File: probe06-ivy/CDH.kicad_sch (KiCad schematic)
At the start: 38 parts, among them J2 Conn_Coaxial, Q1 S9014, U4 NEO-M8M, U5 XBP9B-DPST-001, U6 24LC32, U7 BMP280

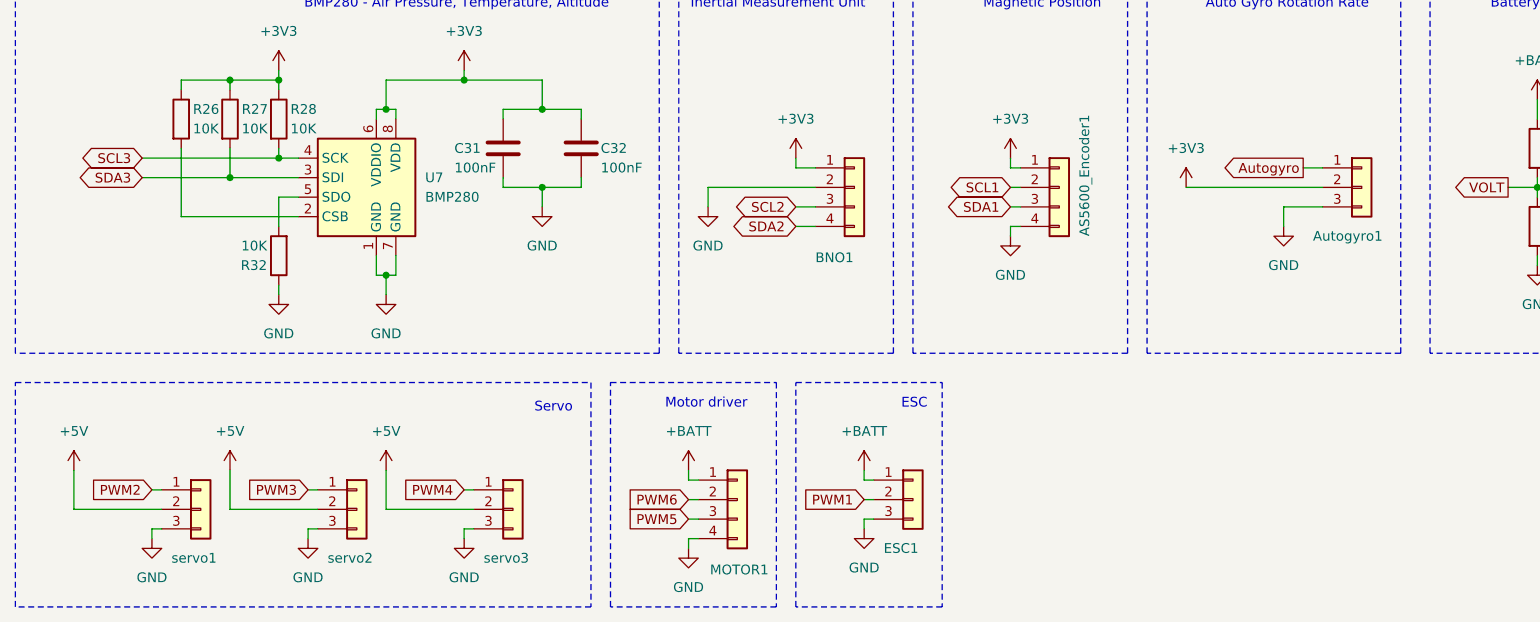
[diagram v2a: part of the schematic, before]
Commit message: Routing (3) Signal routing mostly done with something that needs TODO next: - Correction for power signals - Tidy up component silkscreen - Add team name and tagline
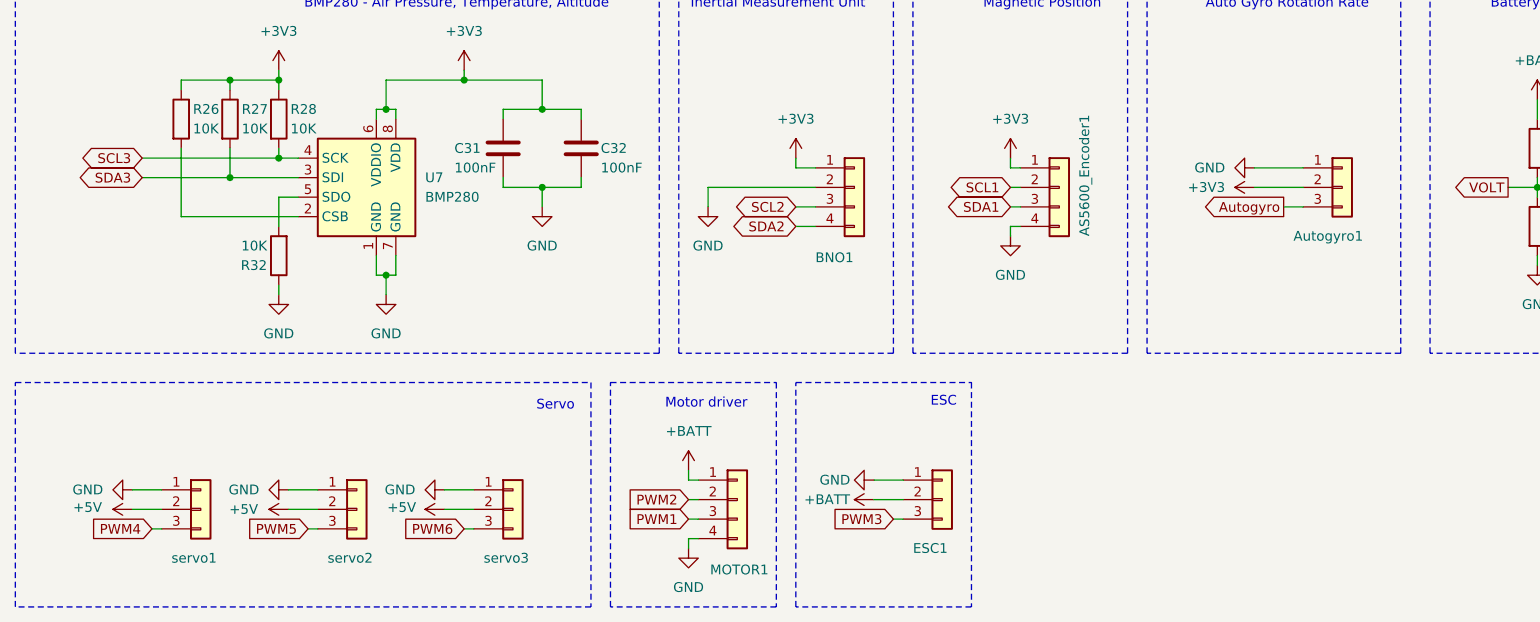
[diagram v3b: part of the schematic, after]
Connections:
- net +BATT: now also ESC1.2 (Pin_2); no longer ESC1.1 (Pin_1)
- net Autogyro: now also Autogyro1.3 (Pin_3); no longer Autogyro1.1 (Pin_1)
- net GND: now also Autogyro1.1 (Pin_1), ESC1.1 (Pin_1), servo1.1 (Pin_1), servo2.1 (Pin_1), servo3.1 (Pin_1); no longer Autogyro1.3 (Pin_3), ESC1.3 (Pin_3), servo1.3 (Pin_3), servo2.3 (Pin_3), servo3.3 (Pin_3)
- net PWM1: now also MOTOR1.3 (Pin_3); no longer ESC1.2 (Pin_2)
- net PWM2: now also MOTOR1.2 (Pin_2); no longer servo1.1 (Pin_1)
- net PWM3: now also ESC1.3 (Pin_3); no longer servo2.1 (Pin_1)
- net PWM4: now also servo1.3 (Pin_3); no longer servo3.1 (Pin_1)
- net PWM5: now also servo2.3 (Pin_3); no longer MOTOR1.3 (Pin_3)
- net PWM6: now also servo3.3 (Pin_3); no longer MOTOR1.2 (Pin_2)
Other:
- moved on the sheet: Autogyro1, ESC1

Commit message: rev 1.2
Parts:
- removed D11: D, Diode_SMD:D_SOD-123, symbol Device:D
- removed R18: 1K, Resistor_SMD:R_0603_1608Metric, symbol Device:R
- renumbered D12 to D10, R19 to R18, R20 to R19, R21 to R20, R22 to R21, R23 to R22, R24 to R23, R25 to R24, R26 to R25, R27 to R26, R28 to R27, R29 to R28, R30 to R29, R31 to R30, R32 to R31

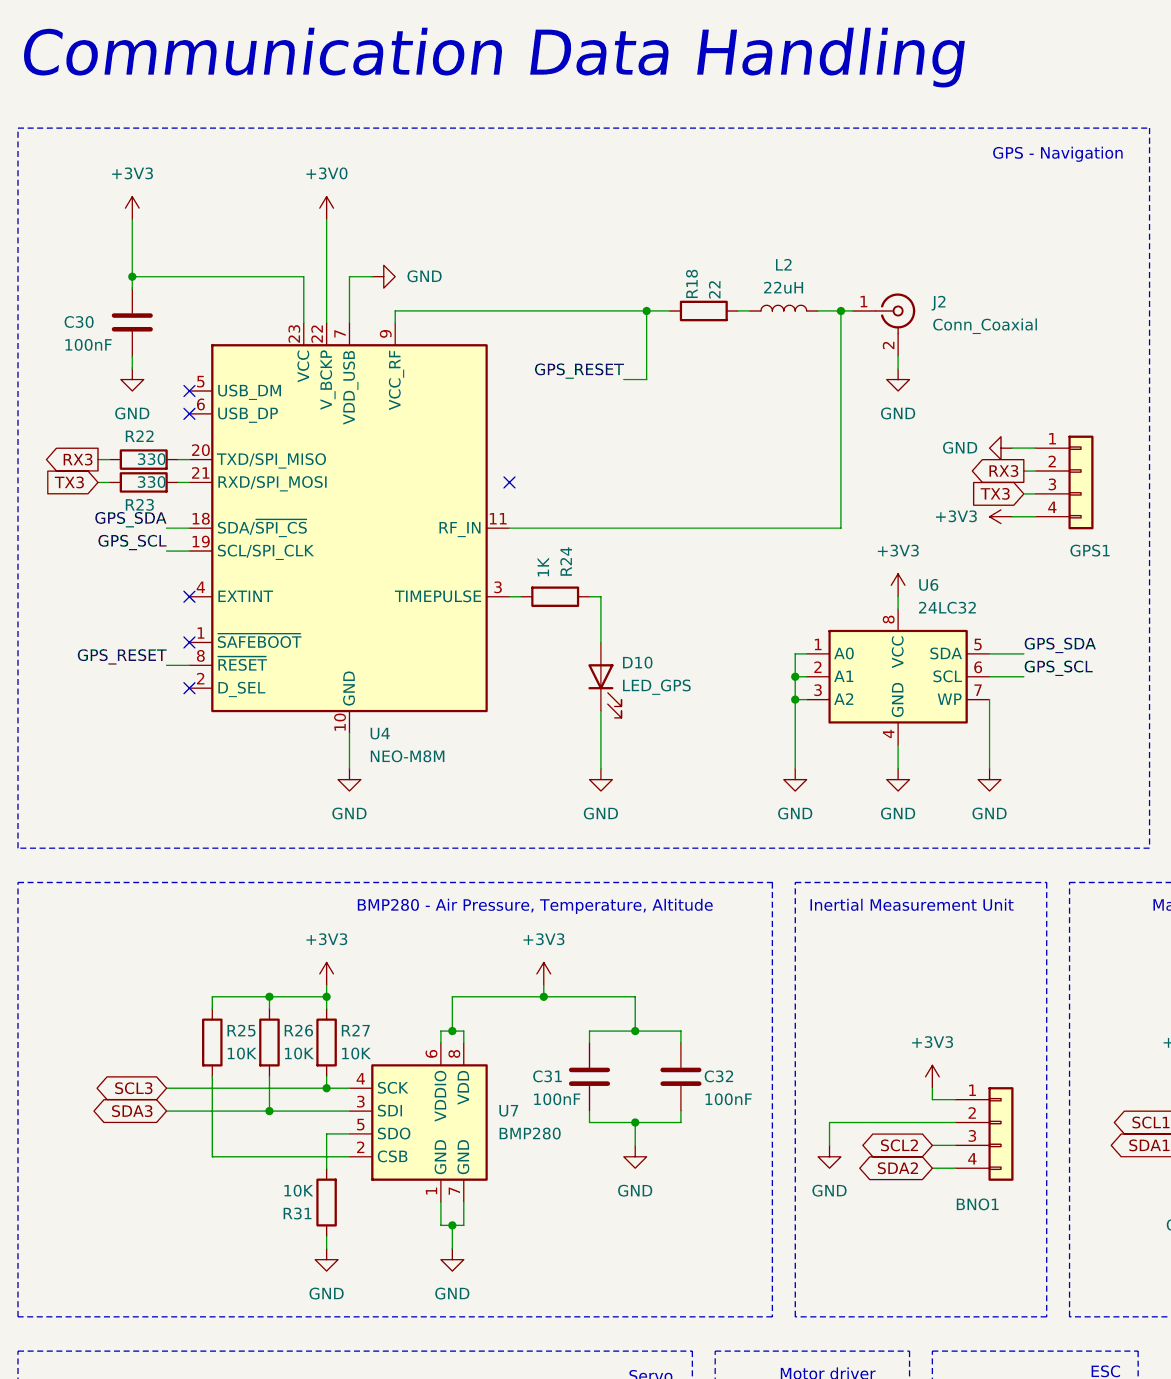
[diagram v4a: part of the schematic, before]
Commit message: rev 1.2.1 add additional pin
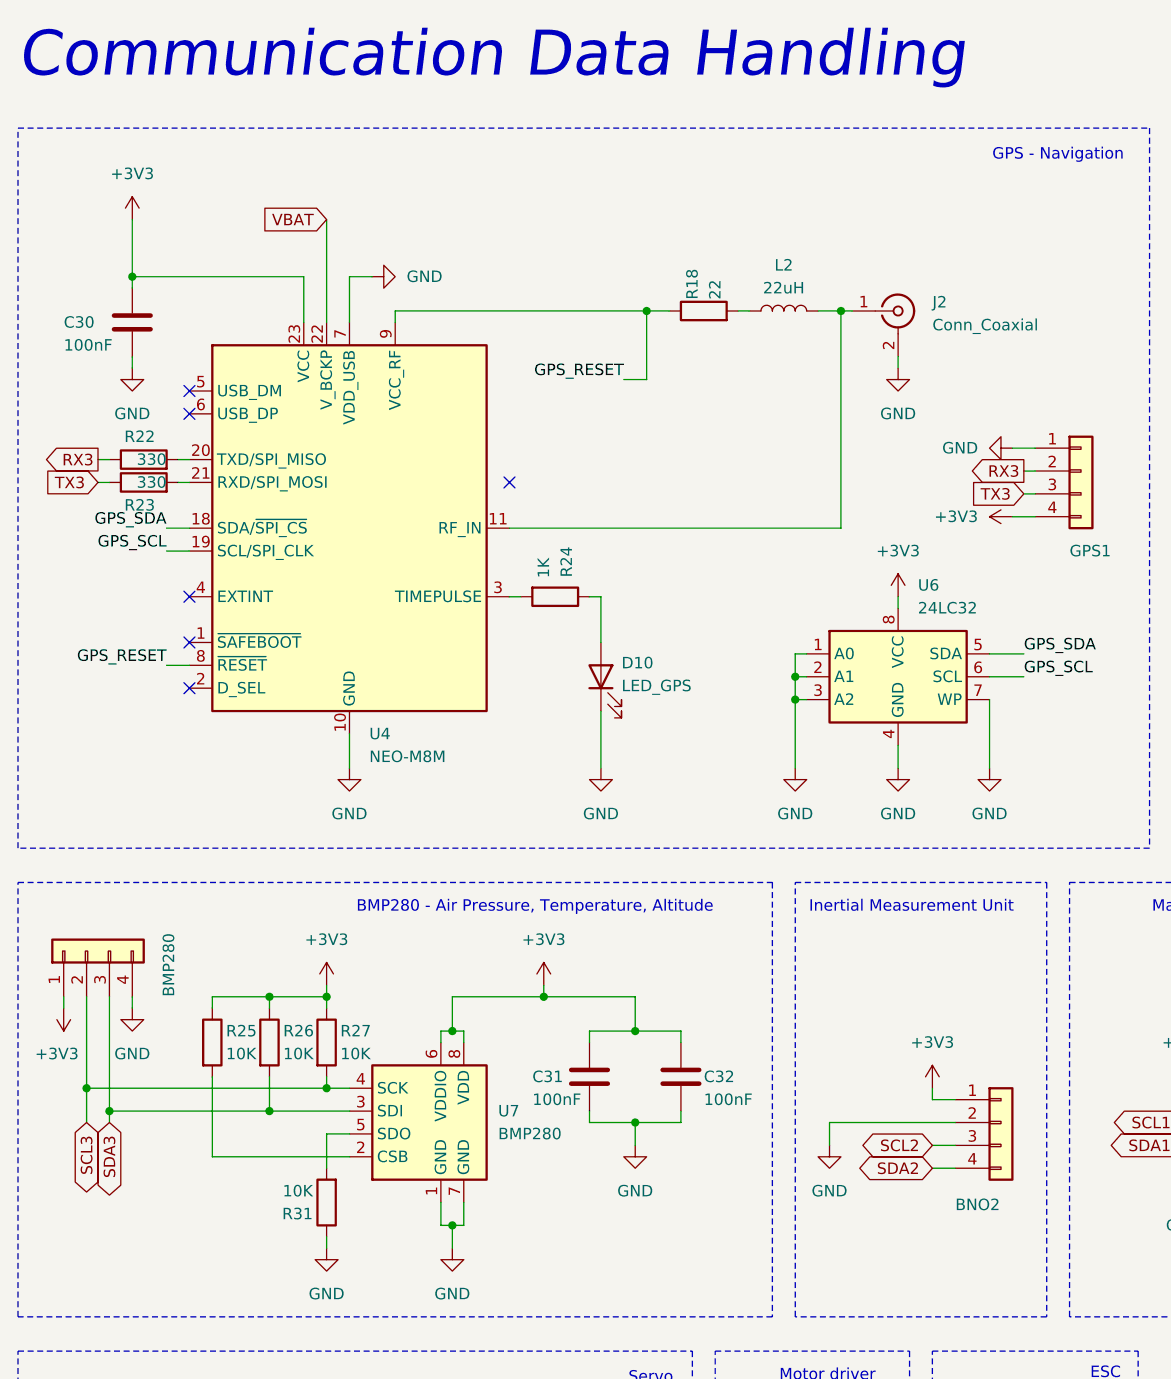
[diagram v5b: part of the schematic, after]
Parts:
- added BMP280: xx, Connector_PinHeader_2.54mm:PinHeader_1x04_P2.54mm_Vertical, symbol Connector_Generic:Conn_01x04
- renumbered BNO1 to BNO2
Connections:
- net +3V3: now also BMP280.1 (Pin_1)
- net GND: now also BMP280.4 (Pin_4)
- net SCL3: now also BMP280.2 (Pin_2)
- net SDA3: now also BMP280.3 (Pin_3)
- net +3V0 renamed VBAT

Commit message: mboh
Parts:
- removed R22, R23: 330, Resistor_SMD:R_0603_1608Metric, symbol Device:R
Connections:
- net RX3: now also U4.20 (TXD/SPI_MISO)
- net TX3: now also U4.21 (RXD/SPI_MOSI)
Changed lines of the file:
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@@
 	(wire
 		(pts
-			(xy 34.29 68.58) (xy 35.56 68.58)
-		)
-		(stroke
-			(width 0)
-			(type default)
-		)
-	)
-	(wire
-		(pts
 			(xy 90.17 130.81) (xy 90.17 129.54)
 		)
@@
 	(wire
 		(pts
-			(xy 25.4 68.58) (xy 26.67 68.58)
+			(xy 25.4 68.58) (xy 35.56 68.58)
 		)
 		(stroke
@@
 	(wire
 		(pts
-			(xy 25.4 66.04) (xy 26.67 66.04)
+			(xy 25.4 66.04) (xy 35.56 66.04)
 		)
 		(stroke
@@
 	(wire
 		(pts
-			(xy 34.29 66.04) (xy 35.56 66.04)
-		)
-		(stroke
-			(width 0)
-			(type default)
-		)
-	)
-	(wire
-		(pts
 			(xy 26.67 138.43) (xy 44.45 138.43)
 		)
@@
 	)
 	(symbol
-		(lib_id "Device:R")
-		(at 30.48 68.58 90)
-		(unit 1)
-		(exclude_from_sim no)
-		(in_bom yes)
-		(on_board yes)
-		(dnp no)
-		(property "Reference" "R23"
-			(at 31.75 71.12 90)
-			(effects
-				(font
-					(size 1.27 1.27)
-				)
-				(justify left)
-			)
-		)
-		(property "Value" "330"
-			(at 33.02 68.58 90)
-			(effects
-				(font
-					(size 1.27 1.27)
-				)
-				(justify left)
-			)
-		)
-		(property "Footprint" "Resistor_SMD:R_0603_1608Metric"
-			(at 30.48 70.358 90)
-			(effects
-				(font
-					(size 1.27 1.27)
-				)
-				(hide yes)
-			)
-		)
-		(property "Datasheet" "~"
-			(at 30.48 68.58 0)
-			(effects
-				(font
-					(size 1.27 1.27)
-				)
-				(hide yes)
-			)
-		)
-		(property "Description" ""
-			(at 30.48 68.58 0)
-			(effects
-				(font
-					(size 1.27 1.27)
-				)
-				(hide yes)
-			)
-		)
-		(pin "1"
-		)
-		(pin "2"
-		)
-		(instances
-			(project "probe06-ivy"
-				(path "/8ec4aa67-98d5-4482-bf96-6c1e71ad8a74/eceef58c-8170-45e6-b9eb-eb38a99a45f6"
-					(reference "R23")
-					(unit 1)
-				)
-			)
-		)
-	)
-	(symbol
 		(lib_name "+3V3_1")
 		(lib_id "power:+3V3")
@@
 					(unit 1)
 				)
-			)
-		)
-	)
-	(symbol
-		(lib_id "Device:R")
-		(at 30.48 66.04 90)
-		(unit 1)
-		(exclude_from_sim no)
-		(in_bom yes)
-		(on_board yes)
-		(dnp no)
-		(property "Reference" "R22"
-			(at 31.75 63.5 90)
-			(effects
-				(font
-					(size 1.27 1.27)
-				)
-				(justify left)
-			)
-		)
-		(property "Value" "330"
-			(at 33.02 66.04 90)
-			(effects
-				(font
-					(size 1.27 1.27)
-				)
-				(justify left)
-			)
-		)
-		(property "Footprint" "Resistor_SMD:R_0603_1608Metric"
-			(at 30.48 67.818 90)
-			(effects
-				(font
-					(size 1.27 1.27)
-				)
-				(hide yes)
-			)
-		)
-		(property "Datasheet" "~"
-			(at 30.48 66.04 0)
-			(effects
-				(font
-					(size 1.27 1.27)
-				)
-				(hide yes)
-			)
-		)
-		(property "Description" ""
-			(at 30.48 66.04 0)
-			(effects
-				(font
-					(size 1.27 1.27)
-				)
-				(hide yes)
-			)
-		)
-		(pin "1"
-		)
-		(pin "2"
-		)
-		(instances
-			(project "probe06-ivy"
-				(path "/8ec4aa67-98d5-4482-bf96-6c1e71ad8a74/eceef58c-8170-45e6-b9eb-eb38a99a45f6"
-					(reference "R22")
-					(unit 1)
-				)
